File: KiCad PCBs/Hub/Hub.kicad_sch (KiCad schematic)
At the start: 22 parts, among them J1 Conn_02x04_Top_Bottom, J2 Conn_02x04_Top_Bottom, U2 RJ45-B-1*4, U3 RJ45-B-1*4

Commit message: Tweaked Hub
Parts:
- R17: LCSC (none) -> C17398
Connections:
- net 12V renamed +12V
- net ACT1 renamed RX_LED1
- net ACT2 renamed RX_LED2
- net ACT3 renamed RX_LED3
- net ACT4 renamed RX_LED4
- net ACT5 renamed RX_LED5
- net ACT6 renamed RX_LED6
- net ACT7 renamed RX_LED7
- net ACT8 renamed RX_LED8
- net PLED1 renamed TX_LED1
- net PLED2 renamed TX_LED2
- net PLED3 renamed TX_LED3
- net PLED4 renamed TX_LED4
- net PLED5 renamed TX_LED5
- net PLED6 renamed TX_LED6
- net PLED7 renamed TX_LED7
- net PLED8 renamed TX_LED8

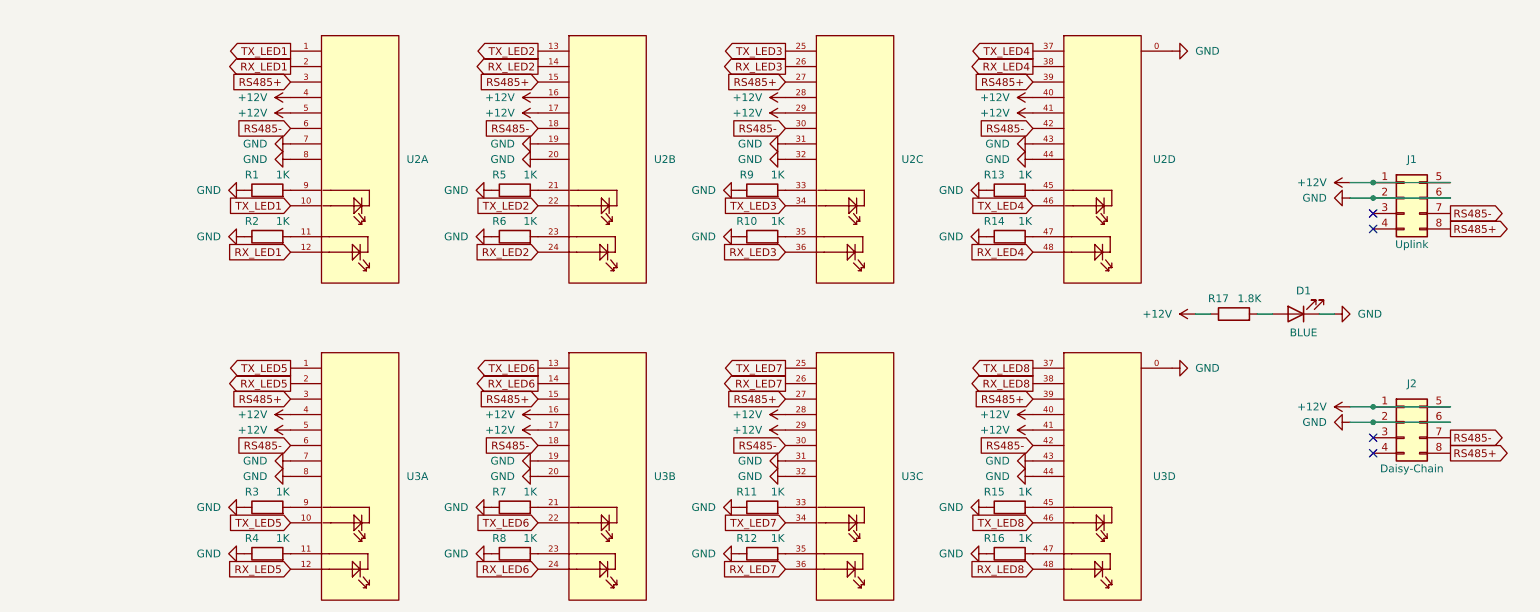
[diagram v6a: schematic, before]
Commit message: Updated TX/RX resistors to 1.8K
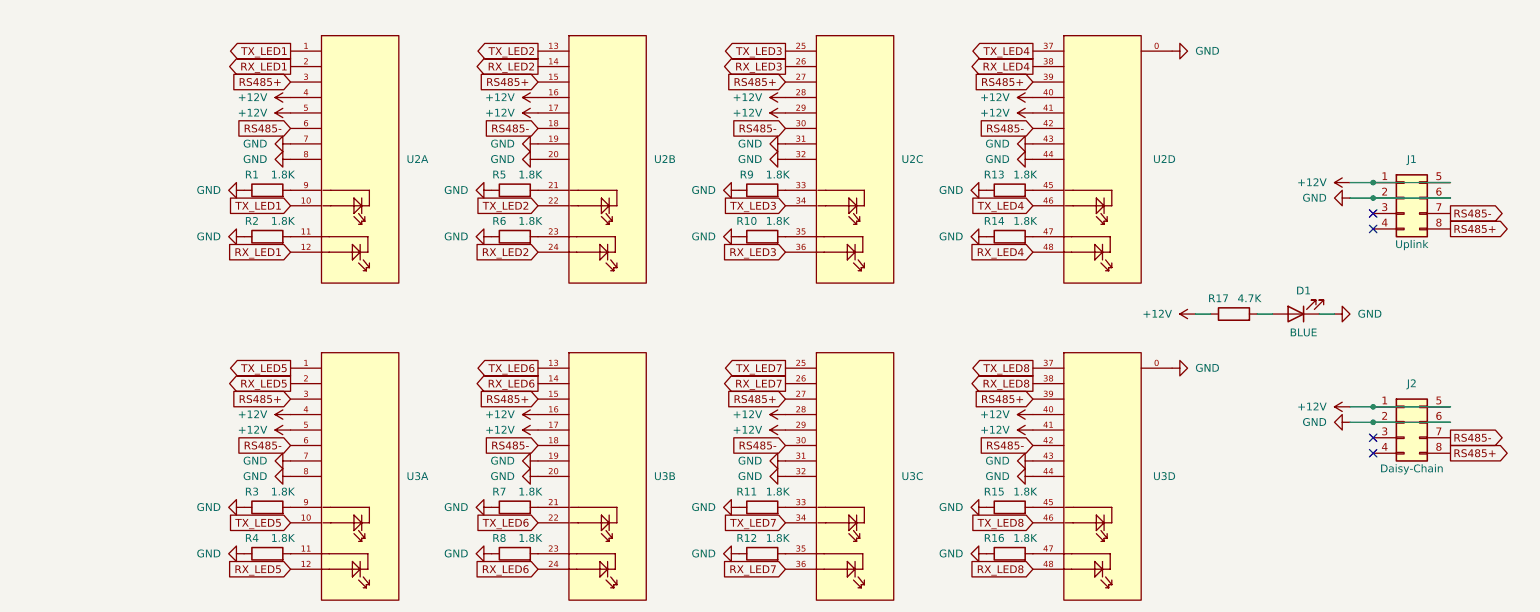
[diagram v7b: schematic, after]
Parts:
- R1, R10, R11, R12, R13, R14, R15, R16, R2, R3, R4, R5, R6, R7, R8, R9: value 1K -> 1.8K; LCSC C17513 -> C17398
- R17: value 1.8K -> 4.7K; LCSC C17398 -> C17673
